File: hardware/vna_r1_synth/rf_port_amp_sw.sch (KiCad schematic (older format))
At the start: 16 parts

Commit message: added passive component test boards, revised coupler
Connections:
- net RF_IN: now also C?.2
- net at U?.1 (RFout): now also C?.2, L?.2
- net at U?.3 (RFin): now also C?.1
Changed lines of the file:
@@
 Wire Wire Line
 	4350 1650 4350 1700
+Wire Wire Line
+	2750 4150 3100 4150
+Wire Wire Line
+	2550 4150 2000 4150
+Wire Wire Line
+	4100 4150 4950 4150
+Wire Wire Line
+	4500 4050 4500 4150
+Connection ~ 4500 4150
 $EndSCHEMATC

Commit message: work on vna r1 synth schematic
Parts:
- added C? (x3): 100 nF, symbol C_Small
- added C? (x2): 10 pF, symbol C_Small
- added C?: 1 uF, symbol C_Small
- added C? (x2): DNP, symbol C_Small
- added R?: 4k7, symbol R_Small
- added R?: 1k2, symbol R_Small
- added R? (x2): JMP, symbol R_Small
- added R?: R_Small, symbol R_Small
- added R?: TBD, symbol R_Small
- added U?: LTC2054CS5, symbol LTC2054CS5
- C? (x5): value C_Small -> 10 pF
- C?: value C_Small -> 100 nF
- R? (x2): value R_Small -> 1k
- R?: value R_Small -> JMP
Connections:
- net -2V5: now also R?.1, U?.2 (V-)
- net AMP_VD: now also L?.1, C?.1, C?.1, C?.1
- net GND: now also U?.2 (NC), U?.5 (NC), U?.6 (NC), U?.7 (GND), C?.2, C?.2, C?.2, C?.2, C?.2, C?.2, R?.1, R?.2
- net at U?.3 (RFC): now also C?.1
- net at C?.1, U?.3 (RFin): now also R?.2
- net at U?.4 (Vc): now also R?.2
- net at R?.1: now also C?.1, R?.1, R?.2
- net at U?.6 (Vout): now also C?.1, R?.1
- new net: R?.2, U?.3 (+IN)
- new net: C?.1, C?.2, R?.2, R?.2, U?.4 (-IN)
- new net +2V5: C?.1, U?.5 (V+)
- new net AMP_VCTL: C?.1, C?.2, R?.1, R?.1, U?.1 (OUT)
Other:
- note added: "typ Ig = 10 uA\nso, burn 500 uA in resistor divider, total of 5k ohms"
- moved on the sheet: C?, L?, R?, U?

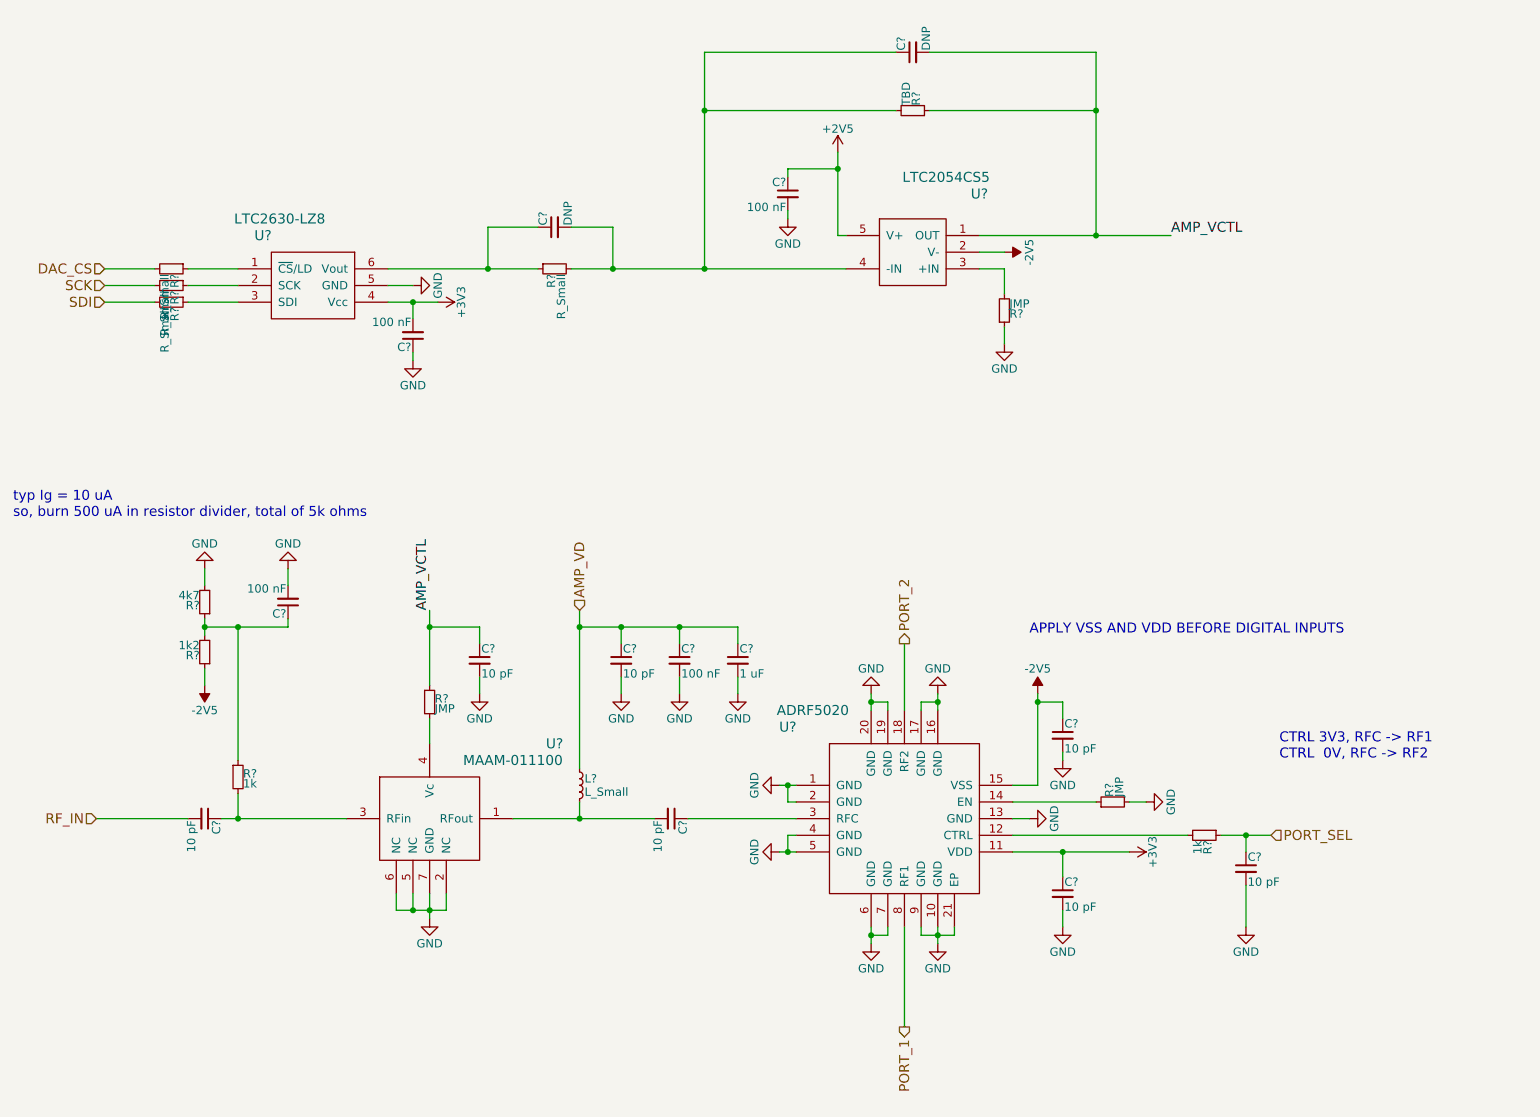
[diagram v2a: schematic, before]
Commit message: ethernet and usb layout on vna control board..
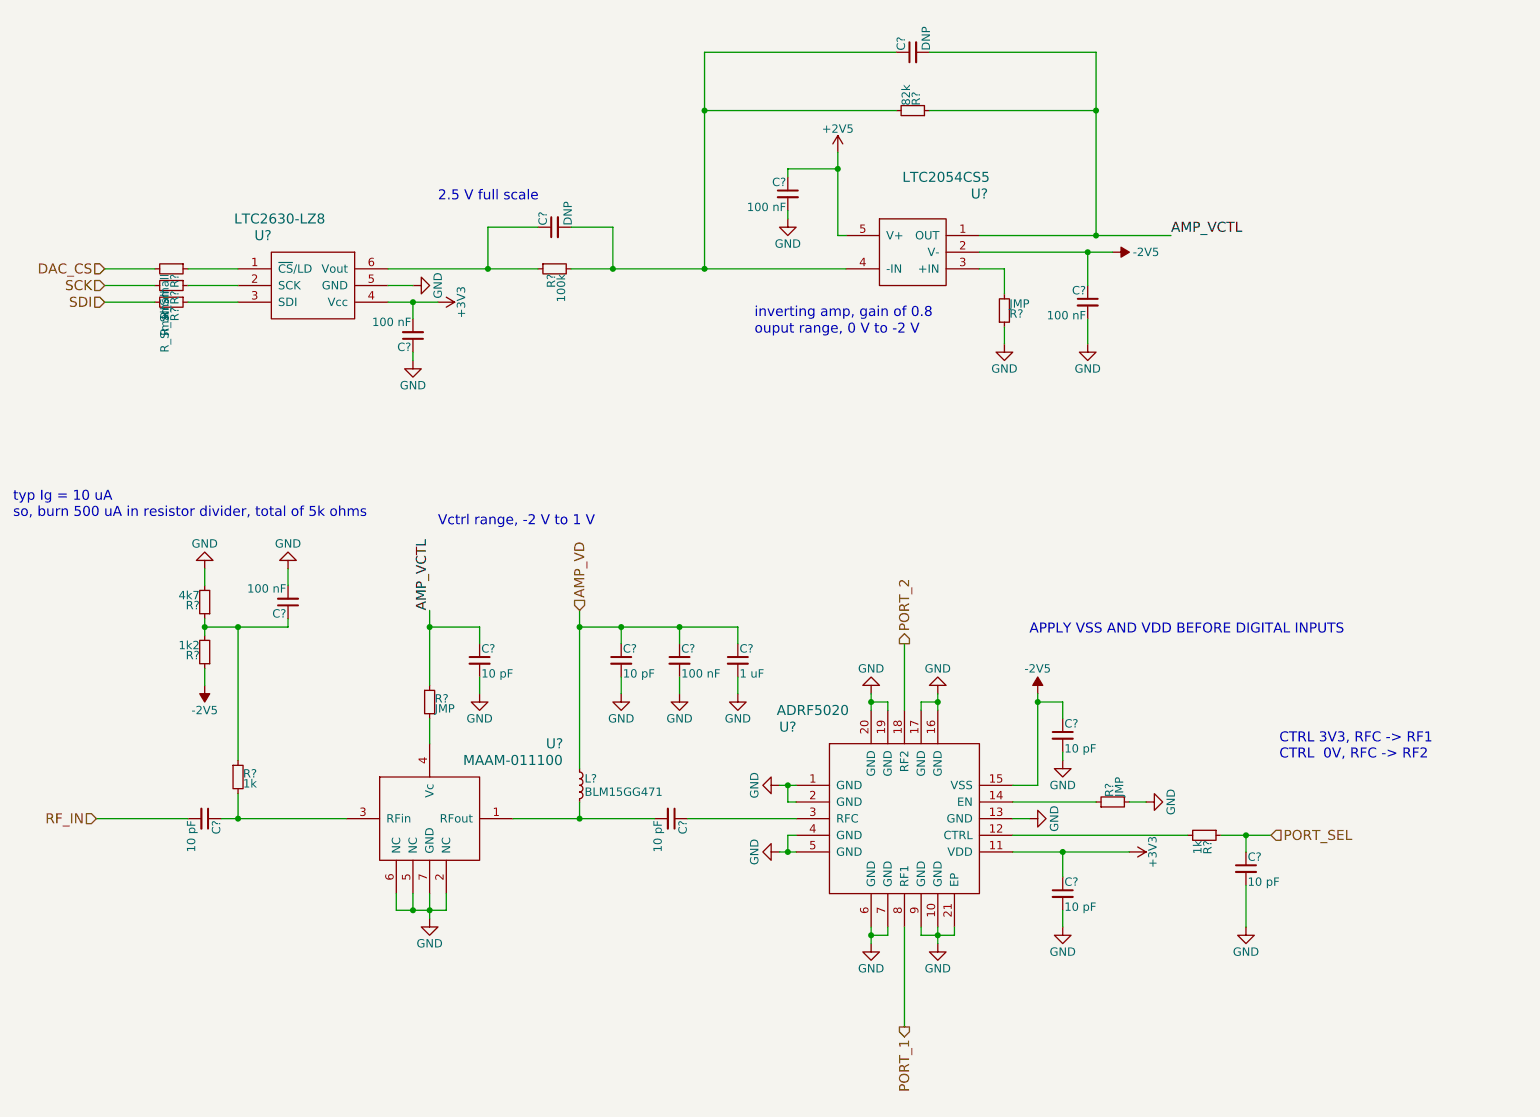
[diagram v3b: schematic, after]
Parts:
- added C?: 100 nF, symbol C_Small
- L?: value L_Small -> BLM15GG471
- R?: value R_Small -> 100k
- R?: value TBD -> 82k
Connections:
- net -2V5: now also C?.1
- net GND: now also C?.2
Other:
- note added: "2.5 V full scale"
- note added: "Vctrl range, -2 V to 1 V"
- note added: "inverting amp, gain of 0.8"
- note added: "ouput range, 0 V to -2 V"
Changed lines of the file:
@@
 P 4250 5150
 F 0 "L?" H 4280 5190 50  0000 L CNN
-F 1 "L_Small" H 4280 5110 50  0000 L CNN
+F 1 "BLM15GG471" H 4280 5110 50  0000 L CNN
 F 2 "" H 4250 5150 50  0001 C CNN
 F 3 "" H 4250 5150 50  0001 C CNN
@@
 L -2V5 #PWR?
 U 1 1 5AC48A14
-P 6800 1950
-F 0 "#PWR?" H 6800 2050 50  0001 C CNN
-F 1 "-2V5" H 6800 2100 50  0000 C CNN
-F 2 "" H 6800 1950 50  0001 C CNN
-F 3 "" H 6800 1950 50  0001 C CNN
-	1    6800 1950
-	0    1    -1   0
-$EndComp
-Wire Wire Line
-	6800 1950 6650 1950
+P 7450 1950
+F 0 "#PWR?" H 7450 2050 50  0001 C CNN
+F 1 "-2V5" V 7450 2150 50  0000 C CNN
+F 2 "" H 7450 1950 50  0001 C CNN
+F 3 "" H 7450 1950 50  0001 C CNN
+	1    7450 1950
+	0    1    1    0
+$EndComp
+Wire Wire Line
+	6650 1950 7450 1950
 $Comp
 L +2V5 #PWR?
@@
 P 4100 2050
 F 0 "R?" H 4130 2070 50  0000 L CNN
-F 1 "R_Small" H 4130 2010 50  0000 L CNN
+F 1 "100k" H 4130 2010 50  0000 L CNN
 F 2 "" H 4100 2050 50  0001 C CNN
 F 3 "" H 4100 2050 50  0001 C CNN
@@
 P 6250 1100
 F 0 "R?" H 6280 1120 50  0000 L CNN
-F 1 "TBD" H 6280 1060 50  0000 L CNN
+F 1 "82k" H 6280 1060 50  0000 L CNN
 F 2 "" H 6250 1100 50  0001 C CNN
 F 3 "" H 6250 1100 50  0001 C CNN
@@
 	4450 1800 4450 2050
 Connection ~ 4450 2050
+Text Notes 3400 3600 0    60   ~ 0
+Vctrl range, -2 V to 1 V
+Text Notes 3400 1650 0    60   ~ 0
+2.5 V full scale
+Text Notes 5300 2350 0    60   ~ 0
+inverting amp, gain of 0.8
+Text Notes 5300 2450 0    60   ~ 0
+ouput range, 0 V to -2 V
+$Comp
+L C_Small C?
+U 1 1 5ACA9A2E
+P 7300 2250
+F 0 "C?" H 7310 2320 50  0000 L CNN
+F 1 "100 nF" H 7310 2170 50  0000 L CNN
+F 2 "" H 7300 2250 50  0001 C CNN
+F 3 "" H 7300 2250 50  0001 C CNN
+	1    7300 2250
+	-1   0    0    -1
+$EndComp
+$Comp
+L GND #PWR?
+U 1 1 5ACA9BCC
+P 7300 2500
+F 0 "#PWR?" H 7300 2250 50  0001 C CNN
+F 1 "GND" H 7300 2350 50  0000 C CNN
+F 2 "" H 7300 2500 50  0001 C CNN
+F 3 "" H 7300 2500 50  0001 C CNN
+	1    7300 2500
+	-1   0    0    -1
+$EndComp
+Wire Wire Line
+	7300 2350 7300 2500
+Wire Wire Line
+	7300 2150 7300 1950
+Connection ~ 7300 1950
 $EndSCHEMATC

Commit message: footprint assignment for vna r1 synth and demod
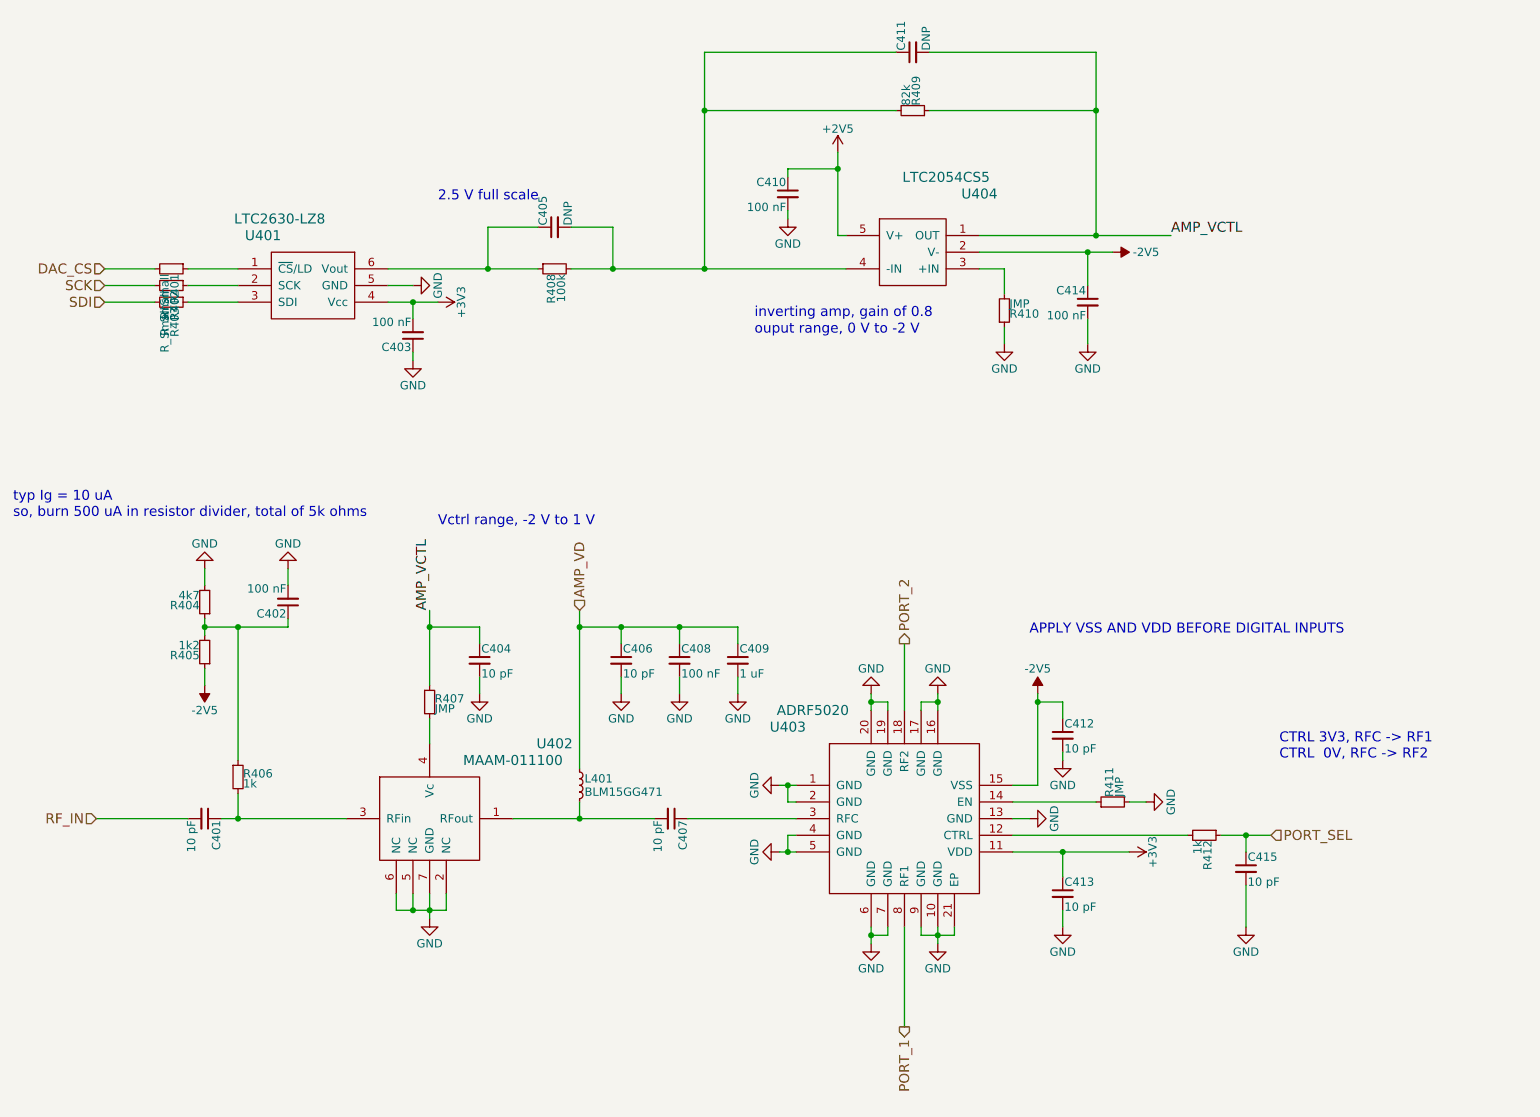
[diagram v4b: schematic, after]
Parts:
- C401, C407: renamed from C?; footprint (none) -> Capacitors_SMD:C_0201
- C402, C403, C404, C405, C406, C408, C409, C410, C411, C412, C413, C414, C415: renamed from C?; footprint (none) -> Capacitors_SMD:C_0402
- L401: renamed from L?; footprint (none) -> Resistors_SMD:R_0402
- R401, R402, R403, R404, R405, R406, R407, R408, R409, R410, R411, R412: renamed from R?; footprint (none) -> Resistors_SMD:R_0402
- U401: renamed from U?; footprint (none) -> TO_SOT_Packages_SMD:SC-70-6
- U402: renamed from U?; footprint (none) -> vna_footprints:TDFN6
- U403: renamed from U?; footprint (none) -> vna_footprints:ADRF5020BCCZN
- U404: renamed from U?; footprint (none) -> TO_SOT_Packages_SMD:SOT-23-5

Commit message: finished vna r1 synth?
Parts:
- R411: value JMP -> 1k
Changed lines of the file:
@@
 $Descr A4 11693 8268
 encoding utf-8
-Sheet 4 5
+Sheet 3 5
 Title ""
 Date ""
@@
 P 7450 5250
 F 0 "R411" H 7480 5270 50  0000 L CNN
-F 1 "JMP" H 7480 5210 50  0000 L CNN
+F 1 "1k" H 7480 5210 50  0000 L CNN
 F 2 "Resistors_SMD:R_0402" H 7450 5250 50  0001 C CNN
 F 3 "" H 7450 5250 50  0001 C CNN
